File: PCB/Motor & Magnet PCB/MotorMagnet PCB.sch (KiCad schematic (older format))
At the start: 46 parts, among them K1 CONN_3, K2 CONN_3

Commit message: KICad BreakOut Board (64 pin DSPic)
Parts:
- gave numbers to parts that had none: 13
- renumbered Current to Current1, Current to Current2, Current to Current3, LED to LED1, R to R16, R to R17, XBEE to XBEE1
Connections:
- wire segments 210 -> 169
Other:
- moved on the sheet: R10, R9

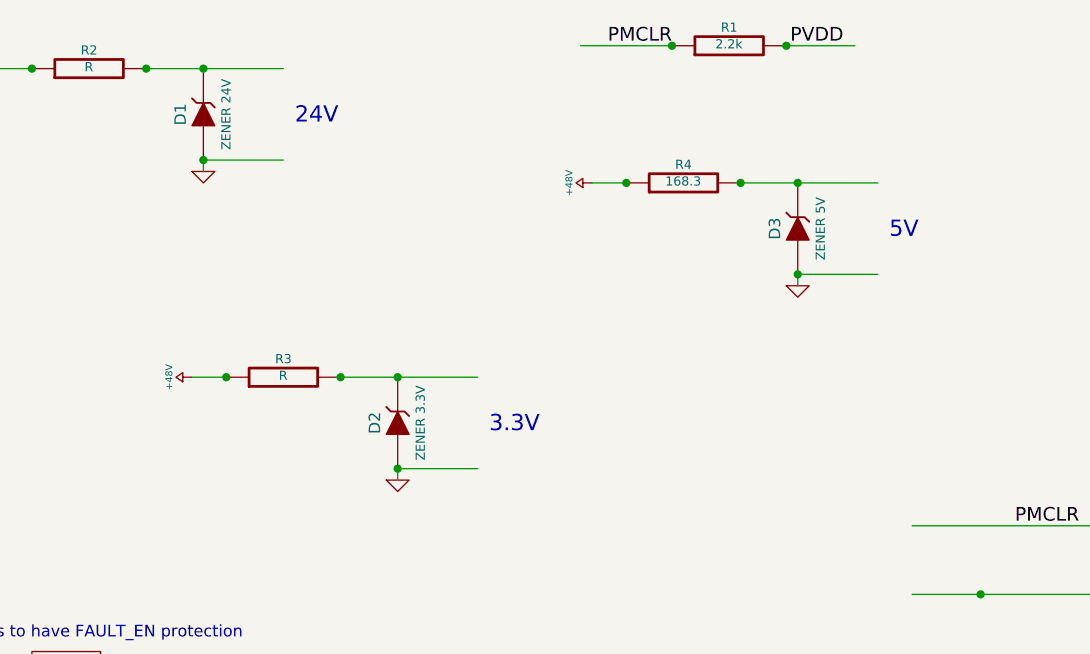
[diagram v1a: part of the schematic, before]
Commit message: Updated Breakout Board 64pin dsPIC
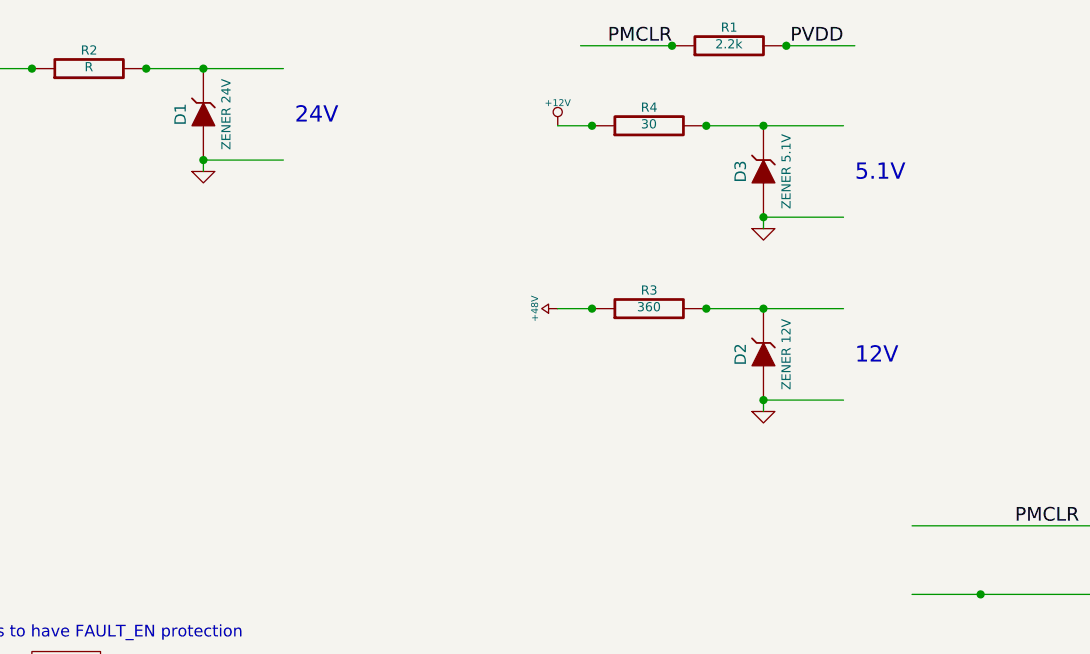
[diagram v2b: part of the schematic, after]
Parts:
- D2: value ZENER 3.3V -> ZENER 12V
- D3: value ZENER 5V -> ZENER 5.1V
- R3: value R -> 360
- R4: value 168.3 -> 30
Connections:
- net labels added: +12V
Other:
- note added: "12V"
- note added: "5.1V"
- note removed: "3.3V"
- note removed: "5V"
- moved on the sheet: D2, D3, R3, R4
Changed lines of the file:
@@
 Sheet 1 1
 Title ""
-Date "2 jul 2013"
+Date "9 jul 2013"
 Rev ""
 Comp ""
@@
 $EndComp
 $Comp
-L +48V #PWR04
-U 1 1 51CCBABA
-P 9800 1600
-F 0 "#PWR04" H 9800 1730 20  0001 C CNN
-F 1 "+48V" H 9800 1700 30  0000 C CNN
-F 2 "" H 9800 1600 60  0000 C CNN
-F 3 "" H 9800 1600 60  0000 C CNN
-	1    9800 1600
-	0    -1   -1   0
-$EndComp
-$Comp
 L R R4
 U 1 1 51CCBB12
-P 10200 1600
-F 0 "R4" V 10280 1600 40  0000 C CNN
-F 1 "168.3" V 10207 1601 40  0000 C CNN
-F 2 "~" V 10130 1600 30  0000 C CNN
-F 3 "~" H 10200 1600 30  0000 C CNN
-	1    10200 1600
+P 10050 1350
+F 0 "R4" V 10130 1350 40  0000 C CNN
+F 1 "30" V 10057 1351 40  0000 C CNN
+F 2 "~" V 9980 1350 30  0000 C CNN
+F 3 "~" H 10050 1350 30  0000 C CNN
+	1    10050 1350
 	0    -1   -1   0
 $EndComp
@@
 L ZENER D3
 U 1 1 51CCBBB5
-P 10700 1800
-F 0 "D3" H 10700 1900 50  0000 C CNN
-F 1 "ZENER 5V" H 10700 1700 40  0000 C CNN
-F 2 "~" H 10700 1800 60  0000 C CNN
-F 3 "~" H 10700 1800 60  0000 C CNN
-	1    10700 1800
+P 10550 1550
+F 0 "D3" H 10550 1650 50  0000 C CNN
+F 1 "ZENER 5.1V" H 10550 1450 40  0000 C CNN
+F 2 "~" H 10550 1550 60  0000 C CNN
+F 3 "~" H 10550 1550 60  0000 C CNN
+	1    10550 1550
 	0    -1   -1   0
 $EndComp
@@
 L GND #PWR05
 U 1 1 51CCBC19
-P 10700 2050
-F 0 "#PWR05" H 10700 2050 30  0001 C CNN
-F 1 "GND" H 10700 1980 30  0001 C CNN
-F 2 "" H 10700 2050 60  0000 C CNN
-F 3 "" H 10700 2050 60  0000 C CNN
-	1    10700 2050
+P 10550 1800
+F 0 "#PWR05" H 10550 1800 30  0001 C CNN
+F 1 "GND" H 10550 1730 30  0001 C CNN
+F 2 "" H 10550 1800 60  0000 C CNN
+F 3 "" H 10550 1800 60  0000 C CNN
+	1    10550 1800
 	1    0    0    -1
 $EndComp
@@
 L +48V #PWR027
 U 1 1 51D1A67A
-P 8050 2450
-F 0 "#PWR027" H 8050 2580 20  0001 C CNN
-F 1 "+48V" H 8050 2550 30  0000 C CNN
-F 2 "" H 8050 2450 60  0000 C CNN
-F 3 "" H 8050 2450 60  0000 C CNN
-	1    8050 2450
+P 9650 2150
+F 0 "#PWR027" H 9650 2280 20  0001 C CNN
+F 1 "+48V" H 9650 2250 30  0000 C CNN
+F 2 "" H 9650 2150 60  0000 C CNN
+F 3 "" H 9650 2150 60  0000 C CNN
+	1    9650 2150
 	0    -1   -1   0
 $EndComp
@@
 L R R3
 U 1 1 51D1A680
-P 8450 2450
-F 0 "R3" V 8530 2450 40  0000 C CNN
-F 1 "R" V 8457 2451 40  0000 C CNN
-F 2 "~" V 8380 2450 30  0000 C CNN
-F 3 "~" H 8450 2450 30  0000 C CNN
-	1    8450 2450
+P 10050 2150
+F 0 "R3" V 10130 2150 40  0000 C CNN
+F 1 "360" V 10057 2151 40  0000 C CNN
+F 2 "~" V 9980 2150 30  0000 C CNN
+F 3 "~" H 10050 2150 30  0000 C CNN
+	1    10050 2150
 	0    -1   -1   0
 $EndComp
@@
 L ZENER D2
 U 1 1 51D1A686
-P 8950 2650
-F 0 "D2" H 8950 2750 50  0000 C CNN
-F 1 "ZENER 3.3V" H 8950 2550 40  0000 C CNN
-F 2 "~" H 8950 2650 60  0000 C CNN
-F 3 "~" H 8950 2650 60  0000 C CNN
-	1    8950 2650
+P 10550 2350
+F 0 "D2" H 10550 2450 50  0000 C CNN
+F 1 "ZENER 12V" H 10550 2250 40  0000 C CNN
+F 2 "~" H 10550 2350 60  0000 C CNN
+F 3 "~" H 10550 2350 60  0000 C CNN
+	1    10550 2350
 	0    -1   -1   0
 $EndComp
@@
 L GND #PWR028
 U 1 1 51D1A68C
-P 8950 2900
-F 0 "#PWR028" H 8950 2900 30  0001 C CNN
-F 1 "GND" H 8950 2830 30  0001 C CNN
-F 2 "" H 8950 2900 60  0000 C CNN
-F 3 "" H 8950 2900 60  0000 C CNN
-	1    8950 2900
+P 10550 2600
+F 0 "#PWR028" H 10550 2600 30  0001 C CNN
+F 1 "GND" H 10550 2530 30  0001 C CNN
+F 2 "" H 10550 2600 60  0000 C CNN
+F 3 "" H 10550 2600 60  0000 C CNN
+	1    10550 2600
 	1    0    0    -1
 $EndComp
@@
 Text Notes 6450 3600 0    51   ~ 0
 Jumper to set all chips to have FAULT_EN protection
-Text Notes 11100 1850 0    71   ~ 0
-5V
-Text Notes 9350 2700 0    71   ~ 0
-3.3V
+Text Notes 10950 1600 0    71   ~ 0
+5.1V
+Text Notes 10950 2400 0    71   ~ 0
+12V
 Text Notes 8500 1350 0    71   ~ 0
 24V
@@
 	15700 7350 15700 7000
 Wire Wire Line
-	9800 1600 9950 1600
-Wire Wire Line
-	10450 1600 11050 1600
-Wire Wire Line
-	10700 2000 11050 2000
-Wire Wire Line
-	10700 2000 10700 2050
+	9650 1350 9800 1350
+Wire Wire Line
+	10300 1350 10900 1350
+Wire Wire Line
+	10550 1750 10900 1750
+Wire Wire Line
+	10550 1750 10550 1800
 Wire Wire Line
 	16550 5500 16550 5650
@@
 Connection ~ 10650 1000
 Connection ~ 10150 1000
-Connection ~ 10700 2000
-Connection ~ 10700 1600
-Connection ~ 9950 1600
-Connection ~ 10450 1600
+Connection ~ 10550 1750
+Connection ~ 10550 1350
+Connection ~ 9800 1350
+Connection ~ 10300 1350
 Connection ~ 18850 6750
 Connection ~ 3100 5500
@@
 Connection ~ 7850 1100
 Wire Wire Line
-	8050 2450 8200 2450
-Wire Wire Line
-	8700 2450 9300 2450
-Wire Wire Line
-	8950 2850 9300 2850
-Wire Wire Line
-	8950 2850 8950 2900
-Connection ~ 8950 2850
-Connection ~ 8950 2450
-Connection ~ 8200 2450
-Connection ~ 8700 2450
+	9650 2150 9800 2150
+Wire Wire Line
+	10300 2150 10900 2150
+Wire Wire Line
+	10550 2550 10900 2550
+Wire Wire Line
+	10550 2550 10550 2600
+Connection ~ 10550 2550
+Connection ~ 10550 2150
+Connection ~ 9800 2150
+Connection ~ 10300 2150
 Connection ~ 15700 6400
 Wire Wire Line
@@
 Wire Wire Line
 	9050 6100 9200 6100
+$Comp
+L +12V #PWR?
+U 1 1 51DC6DFC
+P 9650 1350
+F 0 "#PWR?" H 9650 1300 20  0001 C CNN
+F 1 "+12V" H 9650 1450 30  0000 C CNN
+F 2 "" H 9650 1350 60  0000 C CNN
+F 3 "" H 9650 1350 60  0000 C CNN
+	1    9650 1350
+	1    0    0    -1
+$EndComp
 $EndSCHEMATC
